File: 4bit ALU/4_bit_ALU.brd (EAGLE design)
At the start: 160 x 100 mm, 1 part

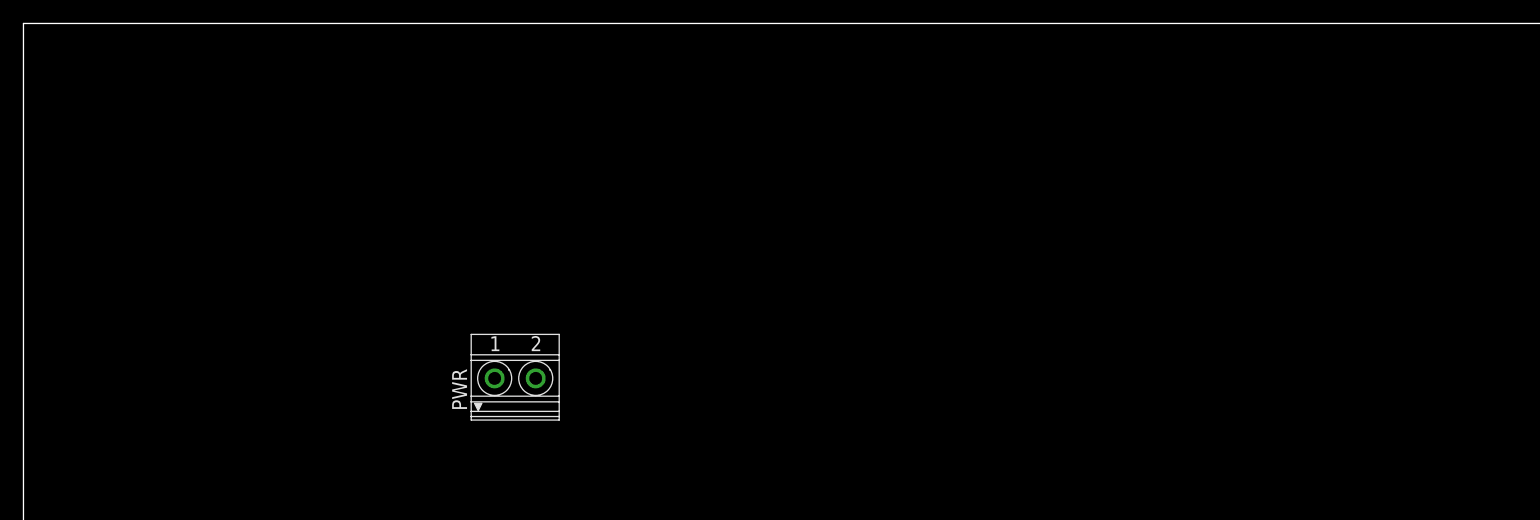
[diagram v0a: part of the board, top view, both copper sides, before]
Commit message: WIP: 4bit ALU. Input and 3-to-8 decoder
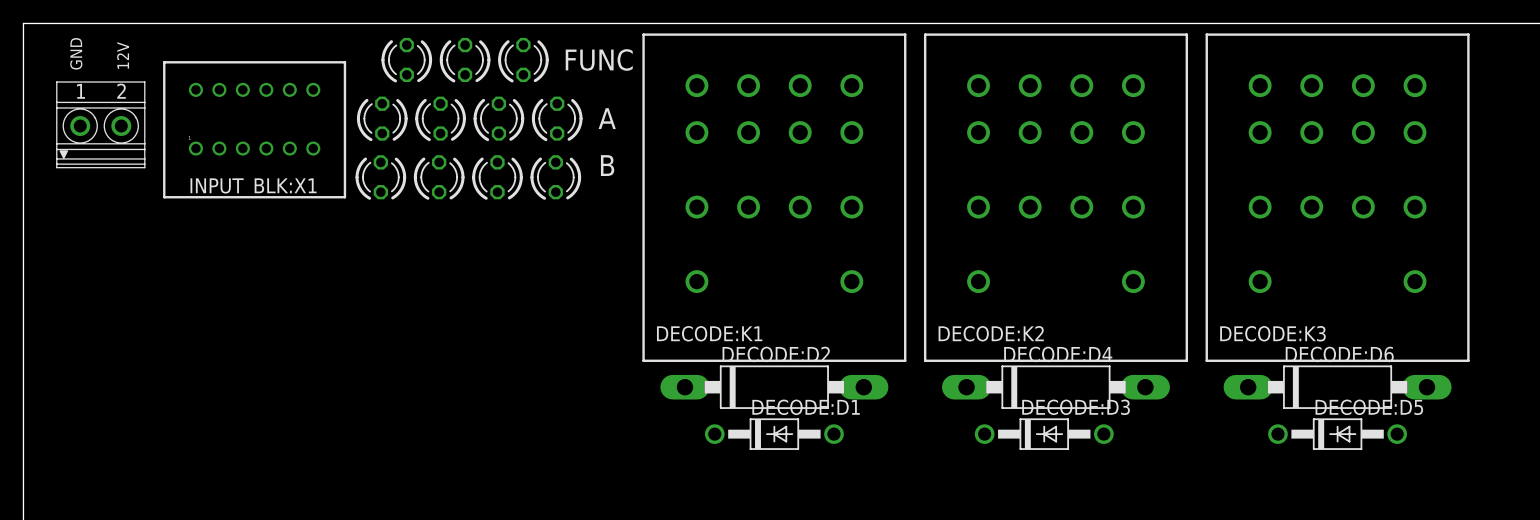
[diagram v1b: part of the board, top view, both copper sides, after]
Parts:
- removed PWR: PWR_BLK, relay_computer_custom:1751248
- added DECODE:D1, DECODE:D3, DECODE:D5: 1N4007, relay_computer_custom:DO41-10
- added DECODE:D2, DECODE:D4, DECODE:D6: 1N5359, relay_computer_custom:C1702-15
- added DECODE:K1, DECODE:K2, DECODE:K3: PY14-02, relay_computer_custom:PY14-02
- added INPUT_BLK:LED1, INPUT_BLK:LED10, INPUT_BLK:LED11, INPUT_BLK:LED2, INPUT_BLK:LED3, INPUT_BLK:LED4, INPUT_BLK:LED5, INPUT_BLK:LED6, INPUT_BLK:LED7, INPUT_BLK:LED8, INPUT_BLK:LED9: (no value), relay_computer_custom:LED3MM
- added INPUT_BLK:X1: 55917-1230, relay_computer_custom:55917-1230
- added PWR_BLK:PWR: PWR_BLK, relay_computer_custom:1751248
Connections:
- new net A0: INPUT_BLK:LED4.A, INPUT_BLK:X1.5
- new net A1: INPUT_BLK:LED5.A, INPUT_BLK:X1.7
- new net A2: INPUT_BLK:LED6.A, INPUT_BLK:X1.9
- new net A3: INPUT_BLK:LED7.A, INPUT_BLK:X1.11
- new net B0: INPUT_BLK:LED8.A, INPUT_BLK:X1.12
- new net B1: INPUT_BLK:LED9.A, INPUT_BLK:X1.10
- new net B2: INPUT_BLK:LED10.A, INPUT_BLK:X1.8
- new net B3: INPUT_BLK:LED11.A, INPUT_BLK:X1.6
- new net DECODE:D$1: DECODE:D1.A, DECODE:D2.A
- new net DECODE:D$2: DECODE:D3.A, DECODE:D4.A
- new net DECODE:D$3: DECODE:D5.A, DECODE:D6.A
- new net DECODE:N$1: DECODE:K1.44, DECODE:K2.41
- new net DECODE:N$2: DECODE:K1.42, DECODE:K2.31
- new net DECODE:N$3: DECODE:K2.44, DECODE:K3.41
- new net DECODE:N$4: DECODE:K2.42, DECODE:K3.31
- new net DECODE:N$5: DECODE:K2.34, DECODE:K3.21
- new net DECODE:N$6: DECODE:K2.32, DECODE:K3.11
- new net ENABLE_CTL0: DECODE:K3.12
- new net ENABLE_CTL1: DECODE:K3.14
- new net ENABLE_CTL2: DECODE:K3.22
- new net ENABLE_CTL3: DECODE:K3.24
- new net ENABLE_CTL4: DECODE:K3.32
- new net ENABLE_CTL5: DECODE:K3.34
- new net ENABLE_CTL6: DECODE:K3.42
- new net ENABLE_CTL7: DECODE:K3.44
- new net FUNC0: DECODE:D1.C, DECODE:K1.A2, INPUT_BLK:LED1.A, INPUT_BLK:X1.2
- new net FUNC1: DECODE:D3.C, DECODE:K2.A2, INPUT_BLK:LED2.A, INPUT_BLK:X1.1
- new net FUNC2: DECODE:D5.C, DECODE:K3.A2, INPUT_BLK:LED3.A, INPUT_BLK:X1.3
- net +12V: now also DECODE:K1.41, PWR_BLK:PWR.2; no longer PWR.2
- net GND: now also DECODE:D2.C, DECODE:D4.C, DECODE:D6.C, DECODE:K1.A1, DECODE:K2.A1, DECODE:K3.A1, INPUT_BLK:LED1.K, INPUT_BLK:LED10.K, INPUT_BLK:LED11.K, INPUT_BLK:LED2.K, INPUT_BLK:LED3.K, INPUT_BLK:LED4.K, INPUT_BLK:LED5.K, INPUT_BLK:LED6.K, INPUT_BLK:LED7.K, INPUT_BLK:LED8.K, INPUT_BLK:LED9.K, PWR_BLK:PWR.1; no longer PWR.1
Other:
- board text added: "12V"
- board text added: "A"
- board text added: "B"
- board text added: "FUNC"
- board text added: "GND"

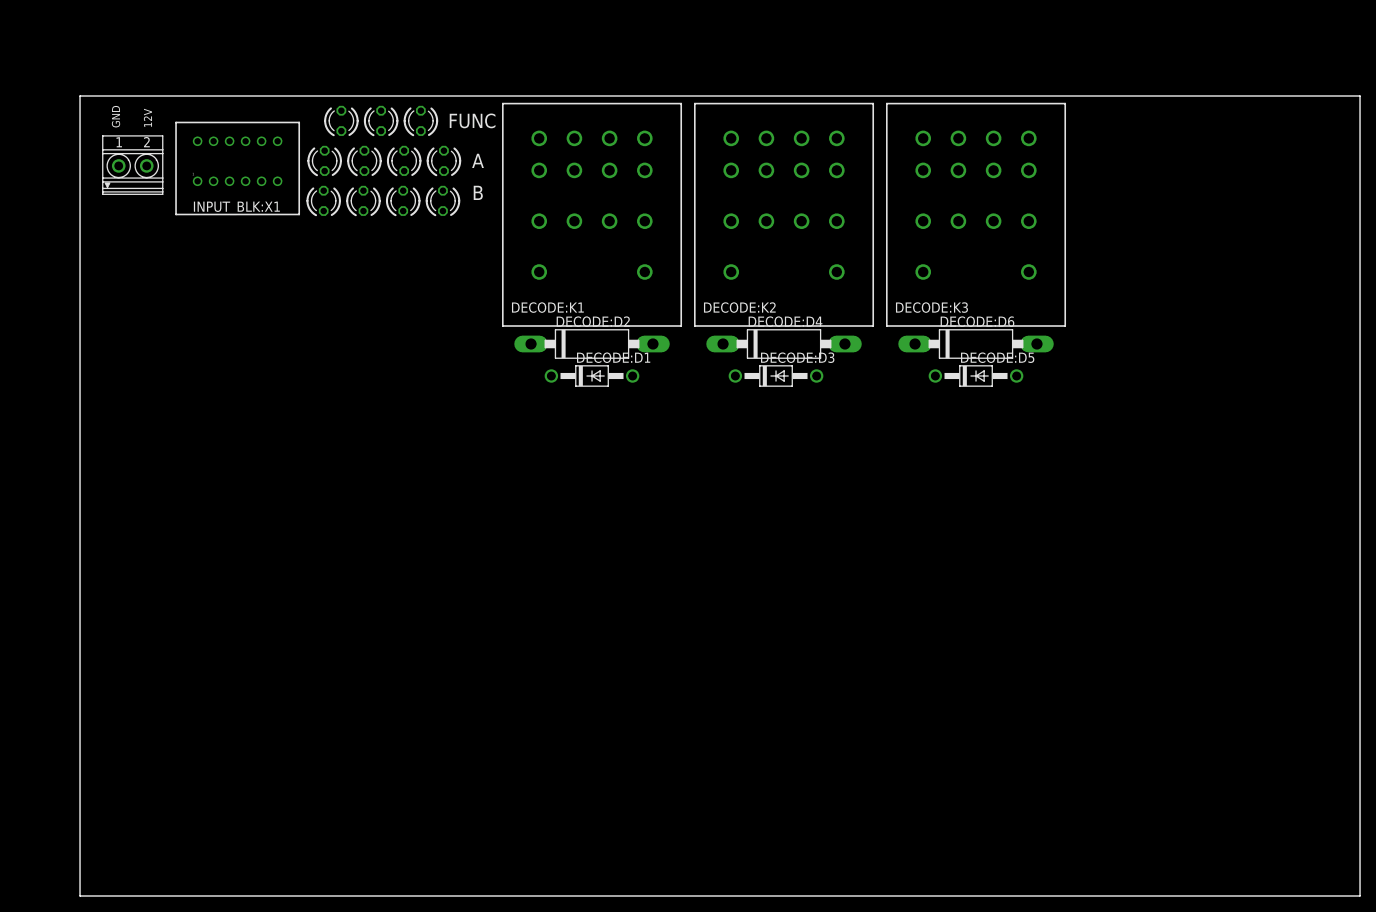
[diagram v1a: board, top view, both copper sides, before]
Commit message: Creating re-usable suppressed relay components w/ vertical diodes
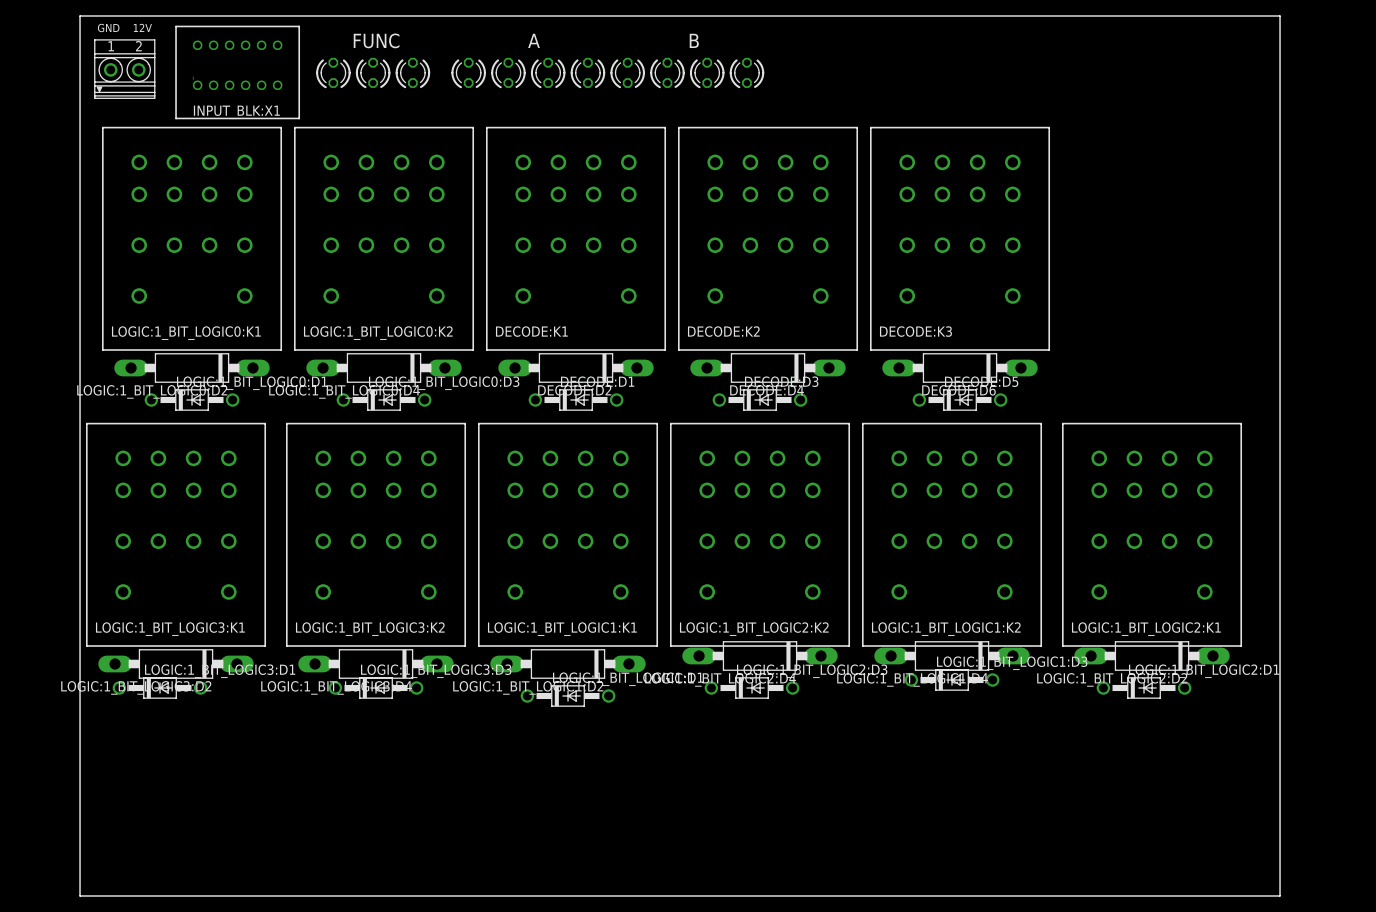
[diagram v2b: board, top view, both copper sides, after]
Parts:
- added LOGIC:1_BIT_LOGIC0:D1, LOGIC:1_BIT_LOGIC0:D3, LOGIC:1_BIT_LOGIC1:D1, LOGIC:1_BIT_LOGIC1:D3, LOGIC:1_BIT_LOGIC2:D1, LOGIC:1_BIT_LOGIC2:D3, LOGIC:1_BIT_LOGIC3:D1, LOGIC:1_BIT_LOGIC3:D3: 1N4007, relay_computer_custom:DO41-10
- added LOGIC:1_BIT_LOGIC0:D2, LOGIC:1_BIT_LOGIC0:D4, LOGIC:1_BIT_LOGIC1:D2, LOGIC:1_BIT_LOGIC1:D4, LOGIC:1_BIT_LOGIC2:D2, LOGIC:1_BIT_LOGIC2:D4, LOGIC:1_BIT_LOGIC3:D2, LOGIC:1_BIT_LOGIC3:D4: 1N5359, relay_computer_custom:C1702-15
- added LOGIC:1_BIT_LOGIC0:K1, LOGIC:1_BIT_LOGIC0:K2, LOGIC:1_BIT_LOGIC1:K1, LOGIC:1_BIT_LOGIC1:K2, LOGIC:1_BIT_LOGIC2:K1, LOGIC:1_BIT_LOGIC2:K2, LOGIC:1_BIT_LOGIC3:K1, LOGIC:1_BIT_LOGIC3:K2: PY14-02, relay_computer_custom:PY14-02
- moved INPUT_BLK:LED10 41.2 mm to (78.4, 102.9)
- moved INPUT_BLK:LED11 41.2 mm to (83.4, 102.9)
- moved INPUT_BLK:LED9 41.2 mm to (73.4, 102.9)
- moved INPUT_BLK:LED8 41.2 mm to (68.5, 102.9)
- moved INPUT_BLK:LED4 21.1 mm to (48.6, 102.9)
- moved INPUT_BLK:LED5 21.1 mm to (53.5, 102.9)
- moved INPUT_BLK:LED6 21.1 mm to (58.5, 102.9)
- moved INPUT_BLK:LED7 21.1 mm to (63.5, 102.9)
- moved PWR_BLK:PWR 12.0 mm to (5.59, 103.4)
- moved INPUT_BLK:X1 12.0 mm to (19.7, 103.8)
- moved INPUT_BLK:LED1 6.08 mm to (31.7, 102.9)
- moved INPUT_BLK:LED2 6.08 mm to (36.6, 102.9)
- moved INPUT_BLK:LED3 6.08 mm to (41.6, 102.9)
- moved DECODE:D1 3.61 mm to (62.0, 62.0)
- moved DECODE:D2 3.61 mm to (62.0, 66.0), turned to 180 degrees
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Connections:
- new net AND0: LOGIC:1_BIT_LOGIC0:K2.11
- new net AND1: LOGIC:1_BIT_LOGIC1:K2.11
- new net AND2: LOGIC:1_BIT_LOGIC2:K2.11
- new net AND3: LOGIC:1_BIT_LOGIC3:K2.11
- new net LOGIC:1_BIT_LOGIC0:D$1: LOGIC:1_BIT_LOGIC0:D1.A, LOGIC:1_BIT_LOGIC0:D2.A
- new net LOGIC:1_BIT_LOGIC0:D$2: LOGIC:1_BIT_LOGIC0:D3.A, LOGIC:1_BIT_LOGIC0:D4.A
- new net LOGIC:1_BIT_LOGIC0:N$1: LOGIC:1_BIT_LOGIC0:K1.44, LOGIC:1_BIT_LOGIC0:K2.14
- new net LOGIC:1_BIT_LOGIC0:N$2: LOGIC:1_BIT_LOGIC0:K1.24, LOGIC:1_BIT_LOGIC0:K2.32
- new net LOGIC:1_BIT_LOGIC0:N$3: LOGIC:1_BIT_LOGIC0:K1.22, LOGIC:1_BIT_LOGIC0:K2.34
- new net LOGIC:1_BIT_LOGIC1:D$1: LOGIC:1_BIT_LOGIC1:D1.A, LOGIC:1_BIT_LOGIC1:D2.A
- new net LOGIC:1_BIT_LOGIC1:D$2: LOGIC:1_BIT_LOGIC1:D3.A, LOGIC:1_BIT_LOGIC1:D4.A
- new net LOGIC:1_BIT_LOGIC1:N$1: LOGIC:1_BIT_LOGIC1:K1.44, LOGIC:1_BIT_LOGIC1:K2.14
- new net LOGIC:1_BIT_LOGIC1:N$2: LOGIC:1_BIT_LOGIC1:K1.24, LOGIC:1_BIT_LOGIC1:K2.32
- new net LOGIC:1_BIT_LOGIC1:N$3: LOGIC:1_BIT_LOGIC1:K1.22, LOGIC:1_BIT_LOGIC1:K2.34
- new net LOGIC:1_BIT_LOGIC2:D$1: LOGIC:1_BIT_LOGIC2:D1.A, LOGIC:1_BIT_LOGIC2:D2.A
- new net LOGIC:1_BIT_LOGIC2:D$2: LOGIC:1_BIT_LOGIC2:D3.A, LOGIC:1_BIT_LOGIC2:D4.A
- new net LOGIC:1_BIT_LOGIC2:N$1: LOGIC:1_BIT_LOGIC2:K1.44, LOGIC:1_BIT_LOGIC2:K2.14
- new net LOGIC:1_BIT_LOGIC2:N$2: LOGIC:1_BIT_LOGIC2:K1.24, LOGIC:1_BIT_LOGIC2:K2.32
- new net LOGIC:1_BIT_LOGIC2:N$3: LOGIC:1_BIT_LOGIC2:K1.22, LOGIC:1_BIT_LOGIC2:K2.34
- new net LOGIC:1_BIT_LOGIC3:D$1: LOGIC:1_BIT_LOGIC3:D1.A, LOGIC:1_BIT_LOGIC3:D2.A
- new net LOGIC:1_BIT_LOGIC3:D$2: LOGIC:1_BIT_LOGIC3:D3.A, LOGIC:1_BIT_LOGIC3:D4.A
- new net LOGIC:1_BIT_LOGIC3:N$1: LOGIC:1_BIT_LOGIC3:K1.44, LOGIC:1_BIT_LOGIC3:K2.14
- new net LOGIC:1_BIT_LOGIC3:N$2: LOGIC:1_BIT_LOGIC3:K1.24, LOGIC:1_BIT_LOGIC3:K2.32
- new net LOGIC:1_BIT_LOGIC3:N$3: LOGIC:1_BIT_LOGIC3:K1.22, LOGIC:1_BIT_LOGIC3:K2.34
- new net NOT0: LOGIC:1_BIT_LOGIC0:K1.42
- new net NOT1: LOGIC:1_BIT_LOGIC1:K1.42
- new net NOT2: LOGIC:1_BIT_LOGIC2:K1.42
- new net NOT3: LOGIC:1_BIT_LOGIC3:K1.42
- new net OR0: LOGIC:1_BIT_LOGIC0:K1.34, LOGIC:1_BIT_LOGIC0:K2.24
- new net OR1: LOGIC:1_BIT_LOGIC1:K1.34, LOGIC:1_BIT_LOGIC1:K2.24
- new net OR2: LOGIC:1_BIT_LOGIC2:K1.34, LOGIC:1_BIT_LOGIC2:K2.24
- new net OR3: LOGIC:1_BIT_LOGIC3:K1.34, LOGIC:1_BIT_LOGIC3:K2.24
- new net XOR0: LOGIC:1_BIT_LOGIC0:K2.31
- new net XOR1: LOGIC:1_BIT_LOGIC1:K2.31
- new net XOR2: LOGIC:1_BIT_LOGIC2:K2.31
- new net XOR3: LOGIC:1_BIT_LOGIC3:K2.31
- net +12V: now also LOGIC:1_BIT_LOGIC0:K1.21, LOGIC:1_BIT_LOGIC0:K1.31, LOGIC:1_BIT_LOGIC0:K1.41, LOGIC:1_BIT_LOGIC0:K2.21, LOGIC:1_BIT_LOGIC1:K1.21, LOGIC:1_BIT_LOGIC1:K1.31, LOGIC:1_BIT_LOGIC1:K1.41, LOGIC:1_BIT_LOGIC1:K2.21, LOGIC:1_BIT_LOGIC2:K1.21, LOGIC:1_BIT_LOGIC2:K1.31, LOGIC:1_BIT_LOGIC2:K1.41, LOGIC:1_BIT_LOGIC2:K2.21, LOGIC:1_BIT_LOGIC3:K1.21, LOGIC:1_BIT_LOGIC3:K1.31, LOGIC:1_BIT_LOGIC3:K1.41, LOGIC:1_BIT_LOGIC3:K2.21
- net A0: now also INPUT_BLK:LED7.A, INPUT_BLK:X1.11, LOGIC:1_BIT_LOGIC0:D1.C, LOGIC:1_BIT_LOGIC0:K1.A2; no longer INPUT_BLK:LED4.A, INPUT_BLK:X1.5
- net A1: now also INPUT_BLK:LED6.A, INPUT_BLK:X1.9, LOGIC:1_BIT_LOGIC1:D1.C, LOGIC:1_BIT_LOGIC1:K1.A2; no longer INPUT_BLK:LED5.A, INPUT_BLK:X1.7
- net A2: now also INPUT_BLK:LED5.A, INPUT_BLK:X1.7, LOGIC:1_BIT_LOGIC2:D1.C, LOGIC:1_BIT_LOGIC2:K1.A2; no longer INPUT_BLK:LED6.A, INPUT_BLK:X1.9
- net A3: now also INPUT_BLK:LED4.A, INPUT_BLK:X1.5, LOGIC:1_BIT_LOGIC3:D1.C, LOGIC:1_BIT_LOGIC3:K1.A2; no longer INPUT_BLK:LED7.A, INPUT_BLK:X1.11
- net B0: now also INPUT_BLK:LED11.A, INPUT_BLK:X1.6, LOGIC:1_BIT_LOGIC0:D3.C, LOGIC:1_BIT_LOGIC0:K2.A2; no longer INPUT_BLK:LED8.A, INPUT_BLK:X1.12
- net B1: now also INPUT_BLK:LED10.A, INPUT_BLK:X1.8, LOGIC:1_BIT_LOGIC1:D3.C, LOGIC:1_BIT_LOGIC1:K2.A2; no longer INPUT_BLK:LED9.A, INPUT_BLK:X1.10
- net B2: now also INPUT_BLK:LED9.A, INPUT_BLK:X1.10, LOGIC:1_BIT_LOGIC2:D3.C, LOGIC:1_BIT_LOGIC2:K2.A2; no longer INPUT_BLK:LED10.A, INPUT_BLK:X1.8
- net B3: now also INPUT_BLK:LED8.A, INPUT_BLK:X1.12, LOGIC:1_BIT_LOGIC3:D3.C, LOGIC:1_BIT_LOGIC3:K2.A2; no longer INPUT_BLK:LED11.A, INPUT_BLK:X1.6
- net FUNC0: now also DECODE:D5.C, DECODE:K3.A2, INPUT_BLK:LED3.A, INPUT_BLK:X1.3; no longer DECODE:D1.C, DECODE:K1.A2, INPUT_BLK:LED1.A, INPUT_BLK:X1.2
- net FUNC2: now also DECODE:D1.C, DECODE:K1.A2, INPUT_BLK:LED1.A, INPUT_BLK:X1.2; no longer DECODE:D5.C, DECODE:K3.A2, INPUT_BLK:LED3.A, INPUT_BLK:X1.3
- net GND: now also LOGIC:1_BIT_LOGIC0:D2.C, LOGIC:1_BIT_LOGIC0:D4.C, LOGIC:1_BIT_LOGIC0:K1.A1, LOGIC:1_BIT_LOGIC0:K2.A1, LOGIC:1_BIT_LOGIC1:D2.C, LOGIC:1_BIT_LOGIC1:D4.C, LOGIC:1_BIT_LOGIC1:K1.A1, LOGIC:1_BIT_LOGIC1:K2.A1, LOGIC:1_BIT_LOGIC2:D2.C, LOGIC:1_BIT_LOGIC2:D4.C, LOGIC:1_BIT_LOGIC2:K1.A1, LOGIC:1_BIT_LOGIC2:K2.A1, LOGIC:1_BIT_LOGIC3:D2.C, LOGIC:1_BIT_LOGIC3:D4.C, LOGIC:1_BIT_LOGIC3:K1.A1, LOGIC:1_BIT_LOGIC3:K2.A1
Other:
- board size 160 x 100 mm -> 150 x 110 mm
